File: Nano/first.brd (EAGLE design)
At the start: 120.6 x 98.7 mm, 17 parts, among them J2 455-1750-1-ND, J3 455-1750-1-ND

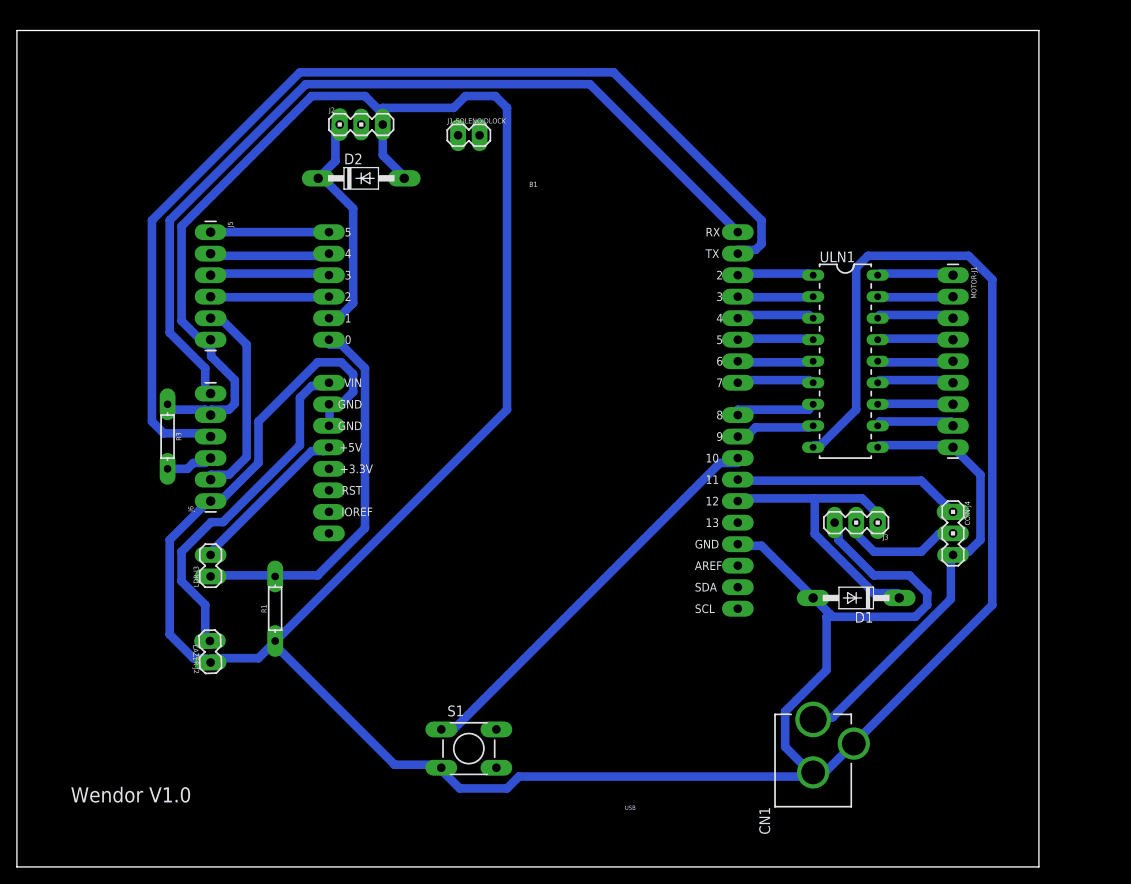
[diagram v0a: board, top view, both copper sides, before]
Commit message: Mini board schematic updated (molex conn added, uno mirrored, tracks and via changed)
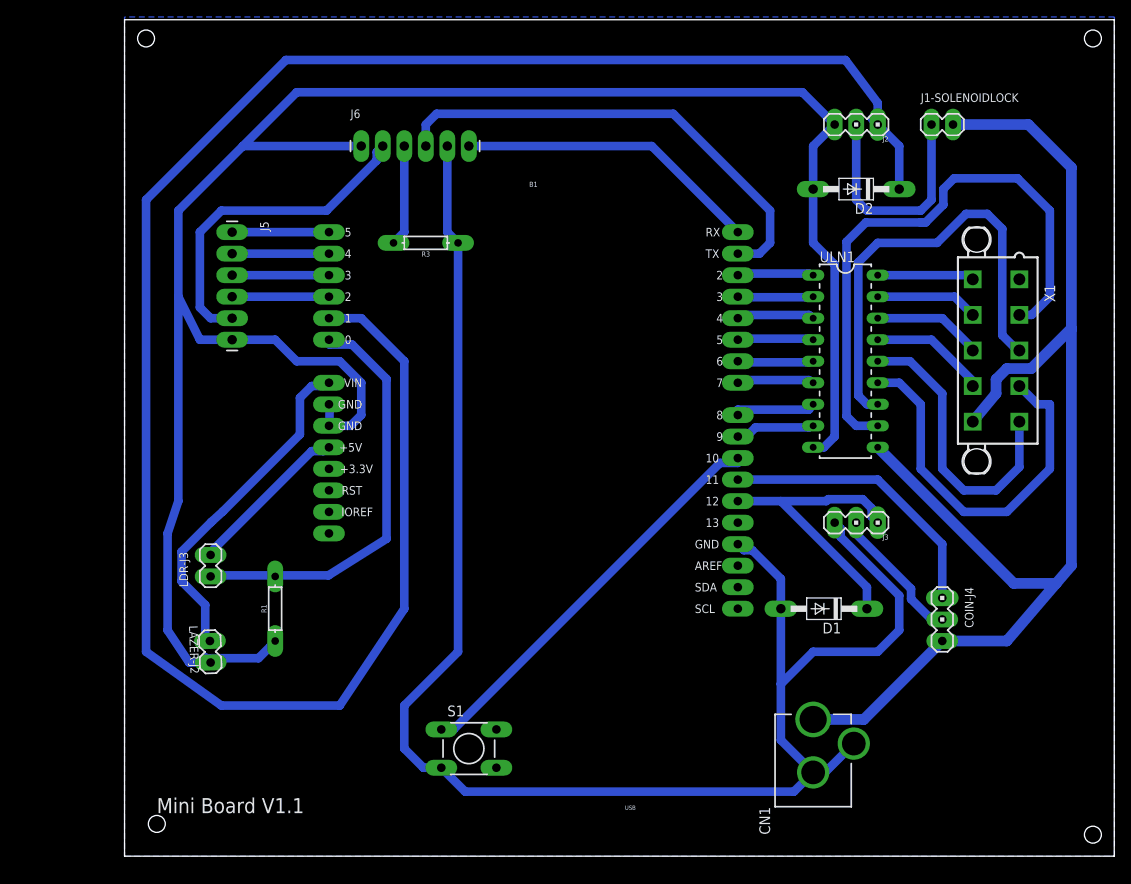
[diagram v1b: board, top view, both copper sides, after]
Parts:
- removed MOTOR-J1: (no value), wendor:1X09_LONGPADS
- added X1: 5566-10, con-molex:5566-10
- moved D2 58.4 mm to (125.7, 74.9), turned to 180 degrees
- moved J2 58.4 mm to (125.7, 82.5), turned to 180 degrees
- moved J1-SOLENOIDLOCK 55.9 mm to (134.6, 82.5)
- moved J6 45.5 mm to (67.3, 80.0), turned to 0 degrees
- moved R3 38.1 mm to (74.9, 68.6), turned to 180 degrees
- moved COIN-J4 10.2 mm to (135.9, 24.1)
- moved D1 4.02 mm to (121.9, 25.4)
- moved J5 2.54 mm to (52.1, 69.8)
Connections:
- net +12V: now also X1.10; no longer MOTOR-J1.9
- net N$10: now also X1.7; no longer MOTOR-J1.2
- net N$11: now also X1.8; no longer MOTOR-J1.3
- net N$12: now also X1.9; no longer MOTOR-J1.4
- net N$13: now also X1.5; no longer MOTOR-J1.5
- net N$14: now also X1.4; no longer MOTOR-J1.6
- net N$15: now also X1.3; no longer MOTOR-J1.7
- net N$16: now also X1.2; no longer MOTOR-J1.8
- net N$9: now also X1.6; no longer MOTOR-J1.1
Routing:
- net N$24: track 28.1 -> 240.1 mm
- net +12V: track 52.8 -> 150.0 mm
- net N$27: track 103.6 -> 36.0 mm
- net N$26: track 124.1 -> 56.6 mm
- net N$16: track 9.52 -> 69.1 mm
- net N$15: track 8.91 -> 53.9 mm
- net GND: track 479.6 -> 442.3 mm
- net N$14: track 9.20 -> 45.3 mm
- net N$25: track 0.00 -> 27.7 mm
- net N$13: track 8.95 -> 34.7 mm
- net N$33: track 24.6 -> 39.6 mm
- net N$22: track 27.0 -> 33.8 mm
- net N$34: track 5.59 -> 12.0 mm
- net N$12: track 8.95 -> 13.8 mm
- net N$17: track 45.5 -> 50.0 mm
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- added copper zone on layer 16, net GND
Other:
- board size 120.6 x 98.7 mm -> 116.8 x 98.7 mm
- board text added: "Mini Board V1.1"
- board text removed: "Wendor V1.0"

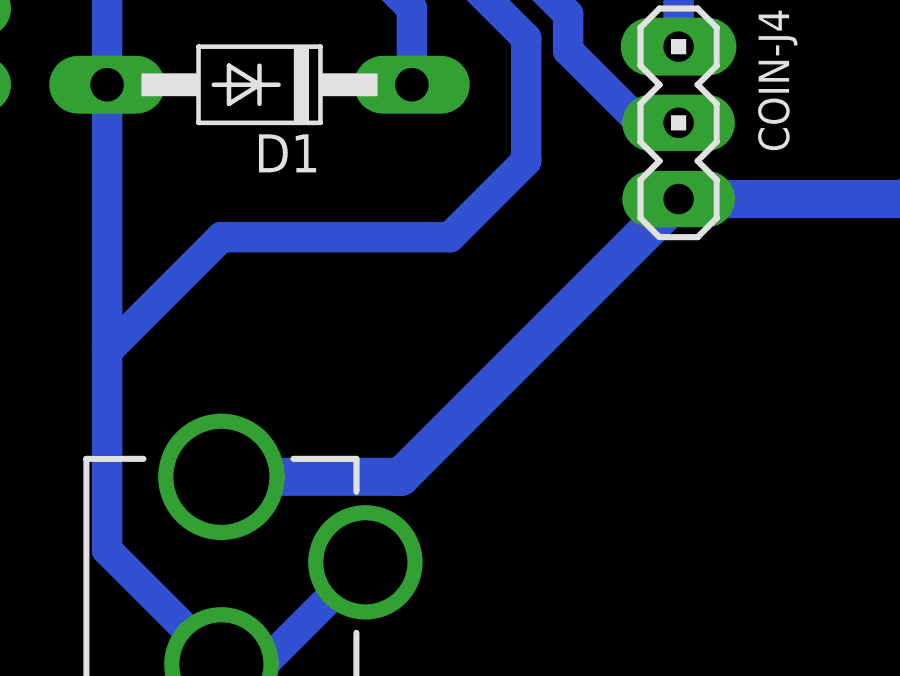
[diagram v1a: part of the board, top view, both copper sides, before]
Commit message: mini board(nano) and lazer-fast pcb modified(DRC errors)
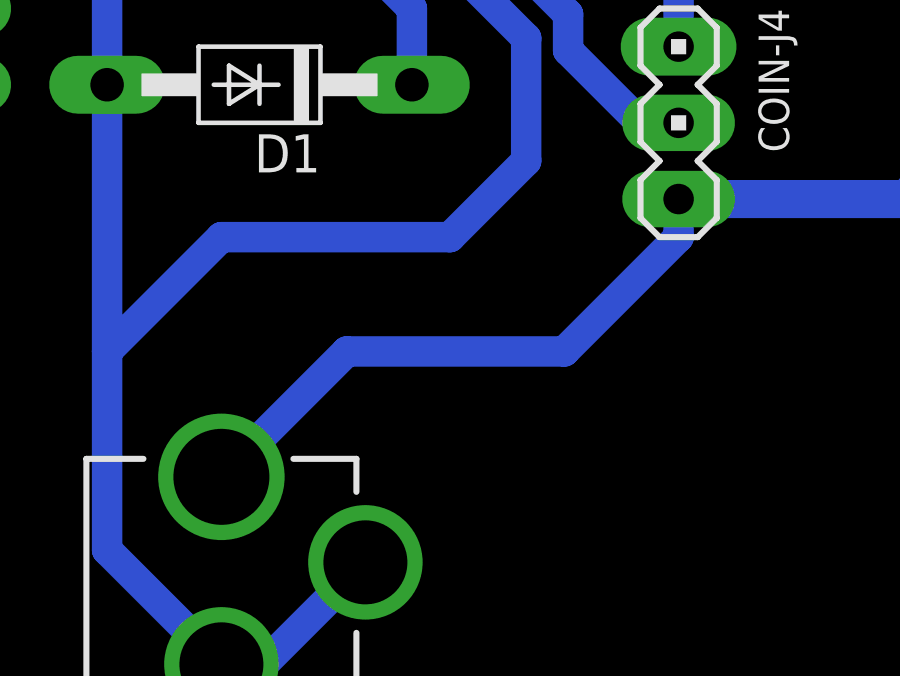
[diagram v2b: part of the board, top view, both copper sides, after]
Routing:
- net +12V: track 150.0 -> 147.3 mm
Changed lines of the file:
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@@
 <setting verticaltext="up"/>
 </settings>
-<grid distance="50" unitdist="mil" unit="mm" style="lines" multiple="1" display="yes" altdistance="5" altunitdist="mil" altunit="mil"/>
+<grid distance="50" unitdist="mil" unit="mil" style="lines" multiple="1" display="yes" altdistance="5" altunitdist="mil" altunit="mil"/>
 <layers>
 <layer number="1" name="Top" color="4" fill="1" visible="yes" active="yes"/>
@@
 <contactref element="CN1" pad="PWR"/>
 <contactref element="J1-SOLENOIDLOCK" pad="2"/>
-<wire x1="124.09" y1="12.33" x2="120.65" y2="12.33" width="1.016" layer="16"/>
 <contactref element="X1" pad="10"/>
 <wire x1="137.16" y1="82.55" x2="146.05" y2="82.55" width="1.27" layer="16"/>
 <wire x1="151.13" y1="77.47" x2="151.13" y2="58.42" width="1.27" layer="16"/>
 <wire x1="151.13" y1="58.42" x2="151.13" y2="30.48" width="1.27" layer="16"/>
-<wire x1="120.65" y1="12.33" x2="126.63" y2="12.33" width="1.27" layer="16"/>
-<wire x1="126.63" y1="12.33" x2="135.89" y2="21.59" width="1.27" layer="16"/>
 <wire x1="143.51" y1="21.59" x2="135.89" y2="21.59" width="1.27" layer="16"/>
 <wire x1="151.13" y1="30.48" x2="149.337059375" y2="28.388234375" width="1.27" layer="16"/>
@@
 <wire x1="146.39284375" y1="53.746" x2="151.06684375" y2="58.42" width="1.27" layer="16"/>
 <wire x1="143.51915625" y1="53.746" x2="146.39284375" y2="53.746" width="1.27" layer="16"/>
+<wire x1="120.65" y1="12.33" x2="124.83" y2="16.51" width="1.016" layer="16"/>
+<wire x1="124.83" y1="16.51" x2="132.08" y2="16.51" width="1.016" layer="16"/>
+<wire x1="132.08" y1="16.51" x2="135.89" y2="20.32" width="1.016" layer="16"/>
+<wire x1="135.89" y1="20.32" x2="135.89" y2="21.59" width="1.016" layer="16"/>
 </signal>
 <signal name="GND">
@@
 </signal>
 </signals>
+<errors>
+</errors>
 </board>
 </drawing>
